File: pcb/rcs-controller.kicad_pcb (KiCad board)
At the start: 2 copper layers, 45.6 x 73 mm, 100 parts, among them J1 00222-32051, J10 0022-232021, J2 0022-232021, J3 0022-232041, J4 Screw_Terminal_4_P3.50mm, J5 USB_C_Receptacle_USB2.0_14P, J6 Conn_01x03, J8 00222-32051, Q1 SI7465DP-T1-E3, Q2 SI7465DP-T1-E3, Q3 SI7465DP-T1-E3, Q4 PMV45EN2, Q5 PMV45EN2, SW1 SW_Push, U1 LSM6DSOX, U2 MP26123DR-LF-Z, U3 TPS63070, U4 ESP32-S3-WROOM-1

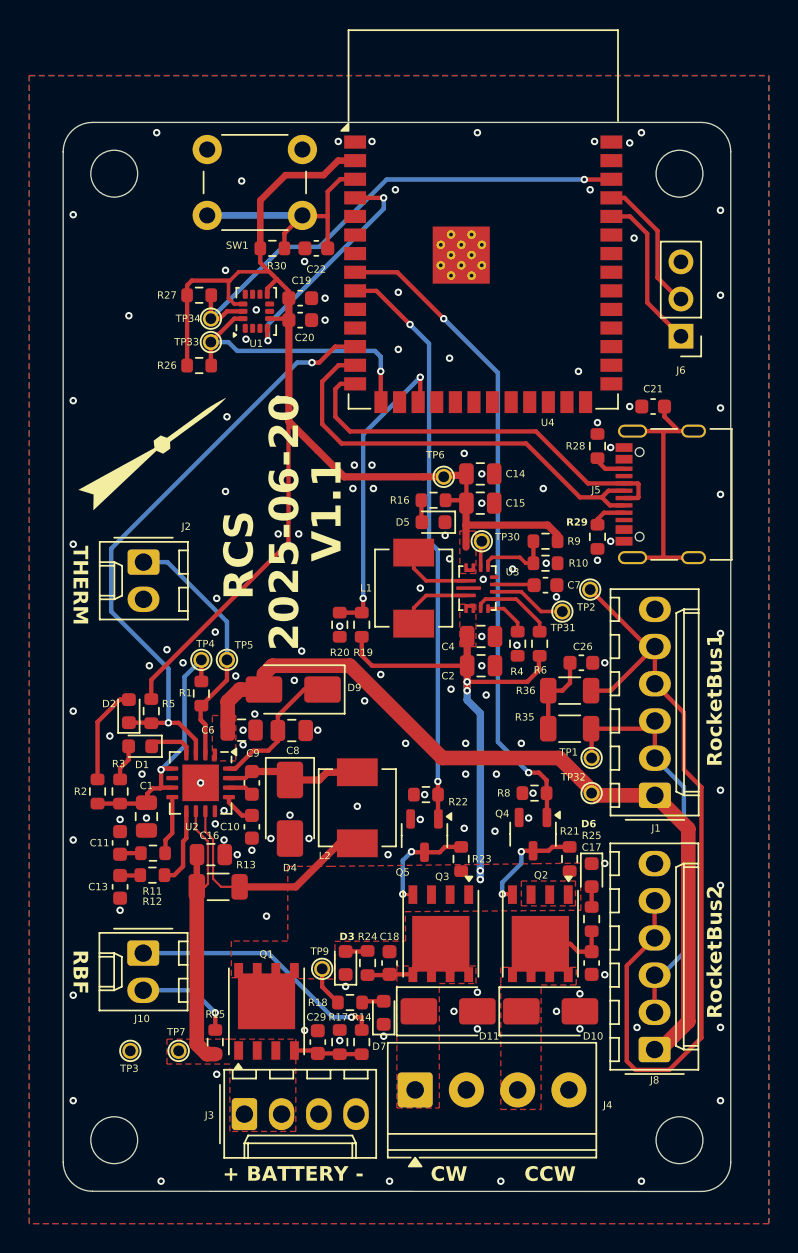
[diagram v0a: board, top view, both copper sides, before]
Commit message: added debug led and boot button
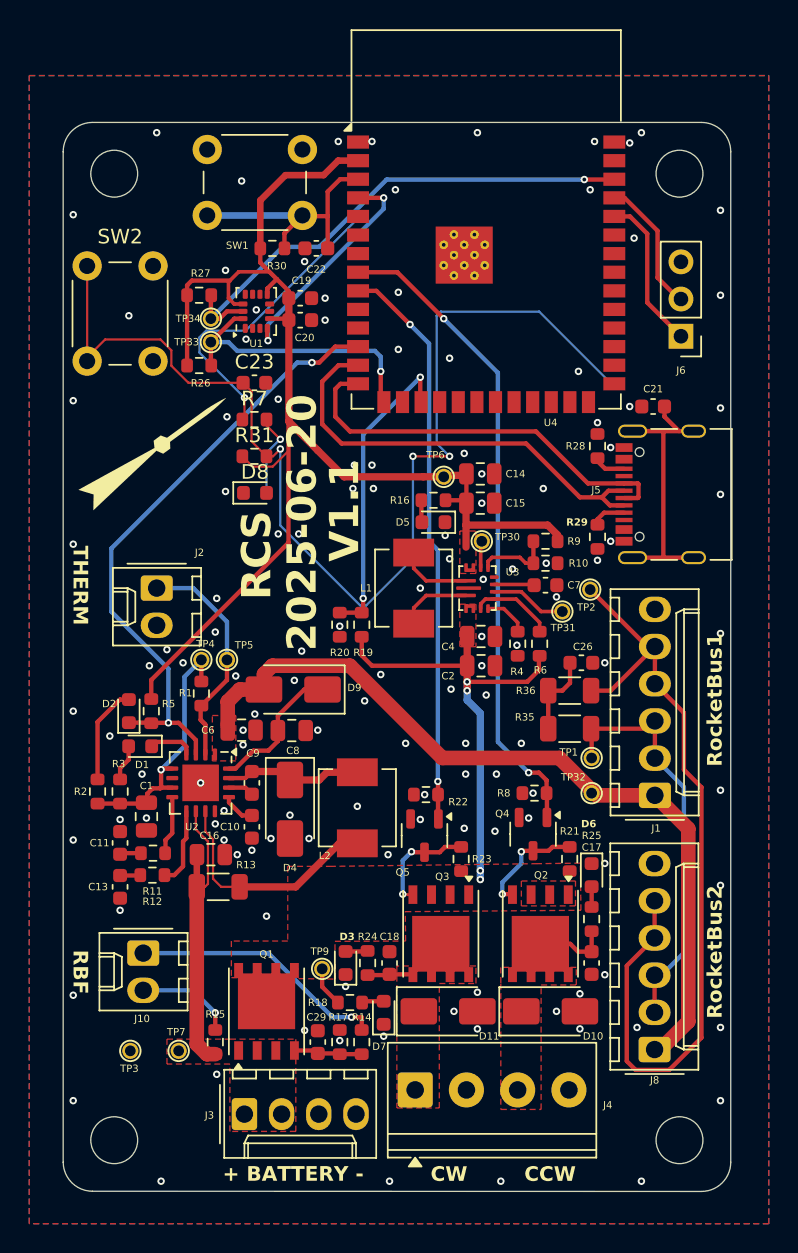
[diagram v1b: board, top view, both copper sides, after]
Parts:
- added C23: 100n, Capacitor_SMD:C_0603_1608Metric, F.Cu at (113.2, 96.0)
- added D8: Red, LED_SMD:LED_0603_1608Metric, F.Cu at (113.2, 103.5)
- added R31: 10k, Resistor_SMD:R_0603_1608Metric, F.Cu at (113.2, 101.0)
- added R7: 4.7, Resistor_SMD:R_0603_1608Metric, F.Cu at (113.2, 98.5)
- added SW2: SW_Push, Button_Switch_THT:SW_PUSH_6mm, F.Cu at (101.8, 94.5)
- C21: value 1p -> 100n
- C22: value 100p -> 100n
- R28, R29: value 5k -> 4.7k
- moved J2 1.99 mm to (106.5, 110.0)
- moved U4 0.20 mm to (129.0, 84.8)
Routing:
- net unconnected-(C23-Pad1): track 0.00 -> 77.7 mm, vias 0 -> 3
- net unconnected-(R7-Pad1): track 0.00 -> 21.5 mm, vias 0 -> 1
- net +3.3V: track 93.2 -> 99.2 mm
- net Net-(D8-A): track 0.00 -> 5.80 mm, vias 0 -> 1
- net Net-(J2-Pin_1): track 17.6 -> 16.0 mm

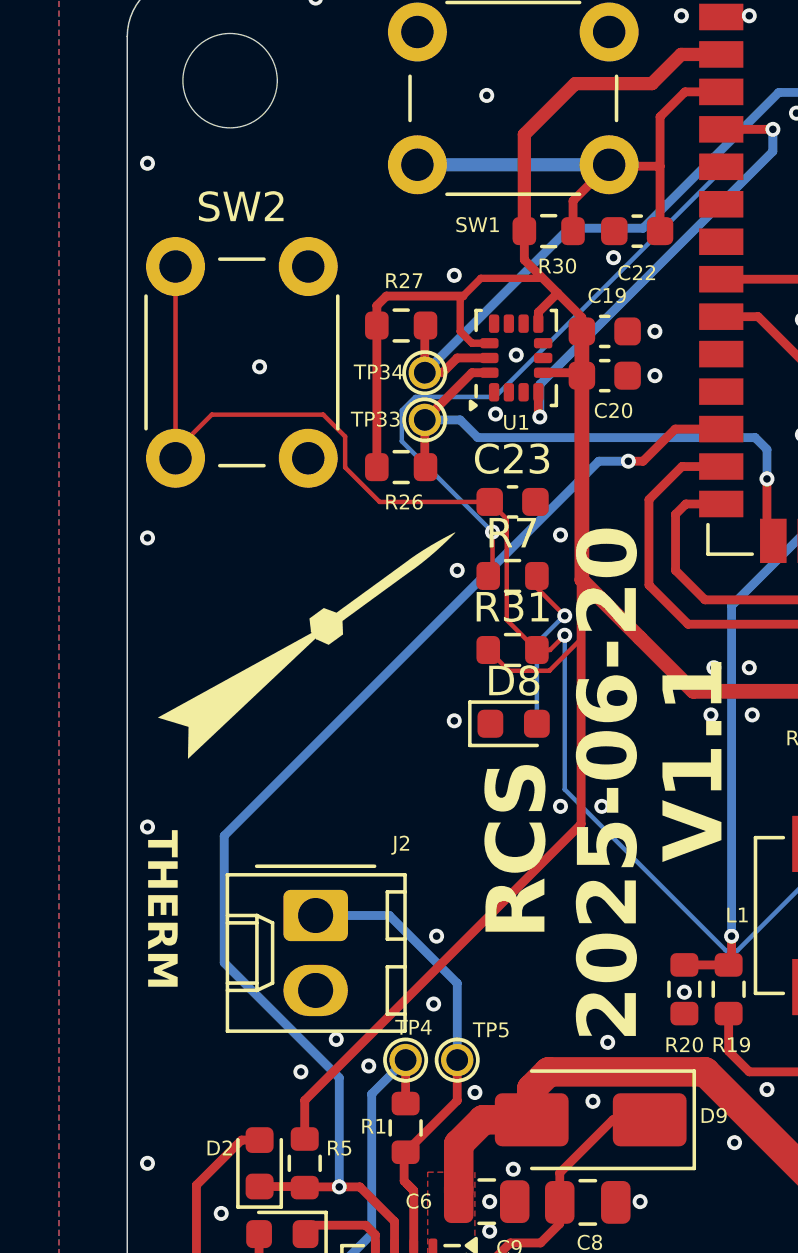
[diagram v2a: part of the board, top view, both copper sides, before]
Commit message: Potential switching circuit between battery and USB
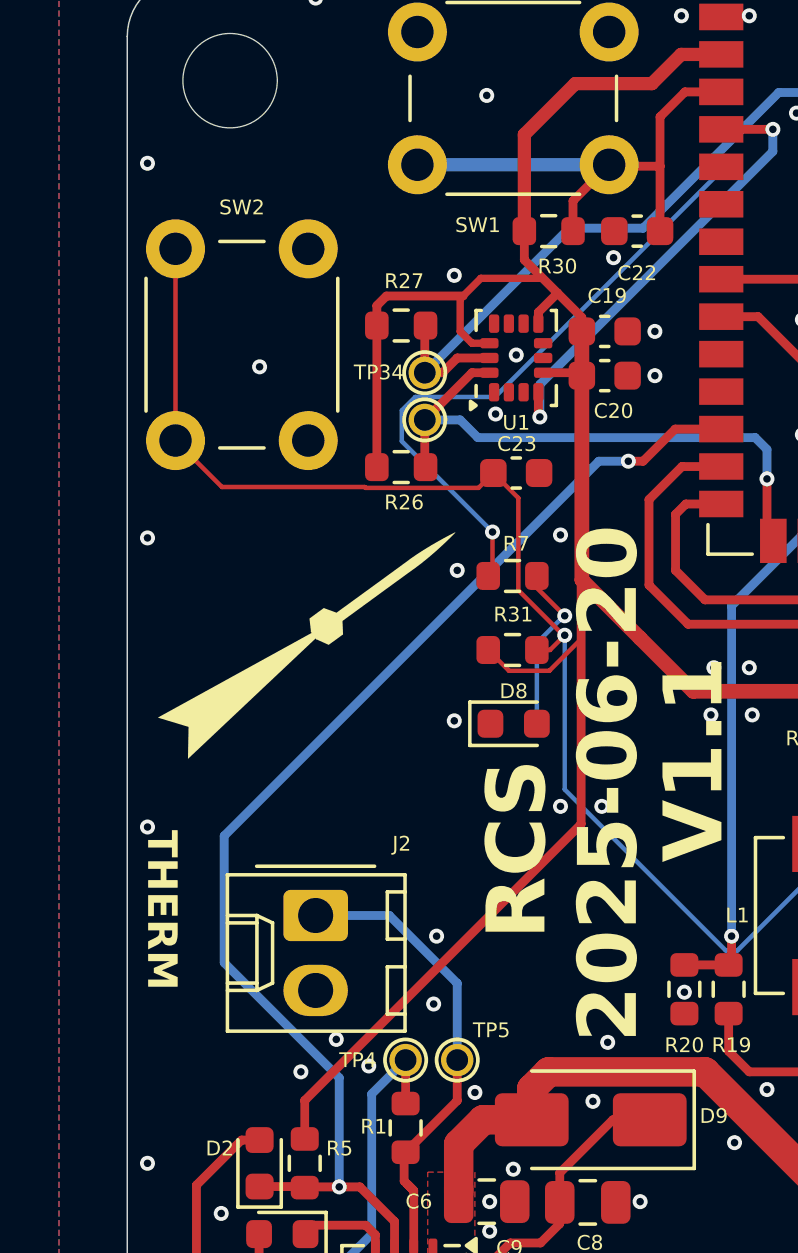
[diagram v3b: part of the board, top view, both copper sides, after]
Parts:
- moved C23 0.99 mm to (113.3, 95.0)
- moved SW2 0.60 mm to (101.8, 93.9)
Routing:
- net unconnected-(C23-Pad1): track 77.7 -> 77.2 mm
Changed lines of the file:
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@@
 		(tags "resistor")
 		(property "Reference" "R31"
-			(at 0 -1.43 0)
+			(at 0.025 -1.2 0)
 			(layer "F.SilkS")
 			(effects
 				(font
-					(size 1 1)
-					(thickness 0.15)
+					(size 0.5 0.5)
+					(thickness 0.125)
 				)
 			)
@@
 		)
 		(fp_text user "${REFERENCE}"
-			(at 0 0 0)
+			(at 0.6 -2.5 0)
 			(layer "F.Fab")
 			(effects
@@
 		(tags "LED")
 		(property "Reference" "D8"
-			(at 0 -1.43 0)
+			(at 0 -1.1 0)
 			(layer "F.SilkS")
 			(effects
 				(font
-					(size 1 1)
-					(thickness 0.15)
+					(size 0.5 0.5)
+					(thickness 0.125)
 				)
 			)
@@
 		(descr "Pin header test point")
 		(property "Reference" "TP4"
-			(at -0.35 -0.8 0)
+			(at -2.25 0.3 0)
 			(layer "F.SilkS")
 			(effects
@@
 	(footprint "Capacitor_SMD:C_0603_1608Metric"
 		(layer "F.Cu")
-		(at 113.175 95.98)
+		(at 113.3 95)
 		(descr "Capacitor SMD 0603 (1608 Metric), square (rectangular) end terminal, IPC-7351 nominal, (Body size source: IPC-SM-782 page 76, https://www.pcb-3d.com/wordpress/wp-content/uploads/ipc-sm-782a_amendment_1_and_2.pdf)")
 		(tags "capacitor")
 		(property "Reference" "C23"
-			(at 0 -1.43 0)
+			(at 0.025 -0.98 0)
 			(layer "F.SilkS")
 			(effects
 				(font
-					(size 1 1)
-					(thickness 0.15)
+					(size 0.5 0.5)
+					(thickness 0.125)
 				)
 			)
@@
 	(footprint "Button_Switch_THT:SW_PUSH_6mm"
 		(layer "F.Cu")
-		(at 101.75 94.5 90)
+		(at 101.75 93.9 90)
 		(descr "Generic 6mm SW tactile push button")
 		(tags "tact sw push 6mm")
 		(property "Reference" "SW2"
-			(at 8.5 2.25 180)
+			(at 7.9 2.25 180)
 			(layer "F.SilkS")
 			(effects
 				(font
-					(size 1 1)
-					(thickness 0.15)
+					(size 0.5 0.5)
+					(thickness 0.125)
 				)
 			)
@@
 		(tags "resistor")
 		(property "Reference" "R7"
-			(at 0 -1.43 0)
+			(at 0.125 -1.09 0)
 			(layer "F.SilkS")
 			(effects
 				(font
-					(size 1 1)
-					(thickness 0.15)
+					(size 0.5 0.5)
+					(thickness 0.125)
 				)
 			)
@@
 			(at -0.3 0.8 180)
 			(layer "F.SilkS")
+			(hide yes)
 			(effects
 				(font
@@
 	)
 	(segment
-		(start 107.5 94.811674)
-		(end 108.668326 95.98)
+		(start 108.191926 95.5036)
+		(end 112.0214 95.5036)
 		(width 0.1524)
 		(layer "F.Cu")
@@
 	)
 	(segment
-		(start 108.668326 95.98)
-		(end 112.4 95.98)
+		(start 113.3714 95.8464)
+		(end 113.3714 98.9714)
 		(width 0.1524)
 		(layer "F.Cu")
@@
 	)
 	(segment
-		(start 102.9786 93.0214)
-		(end 106.758903 93.0214)
+		(start 112.0214 95.5036)
+		(end 112.525 95)
 		(width 0.1524)
 		(layer "F.Cu")
@@
 	)
 	(segment
-		(start 106.758903 93.0214)
-		(end 107.5 93.762497)
+		(start 114.9 100.5)
+		(end 114.9436 100.5)
 		(width 0.1524)
 		(layer "F.Cu")
@@
 	)
 	(segment
-		(start 107.5 93.762497)
-		(end 107.5 94.811674)
+		(start 112.525 95)
+		(end 113.3714 95.8464)
 		(width 0.1524)
 		(layer "F.Cu")
@@
 	)
 	(segment
-		(start 112.4 95.98)
-		(end 112.9786 96.5586)
-		(width 0.1524)
-		(layer "F.Cu")
-		(net "unconnected-(C23-Pad1)")
-	)
-	(segment
 		(start 114 101)
 		(end 114.4436 101)
@@
 	)
 	(segment
-		(start 112.9786 96.5586)
-		(end 112.9786 99.9786)
+		(start 108.162151 95.473825)
+		(end 108.191926 95.5036)
 		(width 0.1524)
 		(layer "F.Cu")
@@
 	)
 	(segment
-		(start 112.9786 99.9786)
-		(end 114 101)
+		(start 113.3714 98.9714)
+		(end 114.9 100.5)
 		(width 0.1524)
 		(layer "F.Cu")
@@
 	)
 	(segment
-		(start 101.75 94.25)
-		(end 102.9786 93.0214)
+		(start 103.323825 95.473825)
+		(end 108.162151 95.473825)
+		(width 0.1524)
+		(layer "F.Cu")
+		(net "unconnected-(C23-Pad1)")
+	)
+	(segment
+		(start 101.75 93.9)
+		(end 103.323825 95.473825)
 		(width 0.1524)
 		(layer "F.Cu")

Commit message: power OR cleanup with Thomas for USB power
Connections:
- C23 pad 1: unconnected-(C23-Pad1) -> Net-(C23-Pad1)
- J5 pad A4: unconnected-(J5-VBUS-PadA4)_1 -> +5V
- J5 pad A9: unconnected-(J5-VBUS-PadA4)_2 -> +5V
- J5 pad B4: unconnected-(J5-VBUS-PadA4) -> +5V
- J5 pad B9: unconnected-(J5-VBUS-PadA4)_3 -> +5V
- R28 pad 1: Net-(J5-CC2) -> Net-(J5-CC1)
- R29 pad 1: Net-(J5-CC1) -> Net-(J5-CC2)
- R31 pad 2: unconnected-(C23-Pad1) -> Net-(C23-Pad1)
- R7 pad 1: unconnected-(R7-Pad1) -> Net-(U4-IO5)
- SW2 pad 1: unconnected-(C23-Pad1) -> Net-(U4-IO0)
- U4 pad 27: unconnected-(C23-Pad1) -> Net-(U4-IO0)
- U4 pad 5: unconnected-(R7-Pad1) -> Net-(U4-IO5)
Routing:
- net unconnected-(C23-Pad1): track 77.2 -> 0.00 mm, vias 3 -> 0
- net (no net): track 0.00 -> 77.2 mm, vias 0 -> 3
- net unconnected-(R7-Pad1): track 21.5 -> 0.00 mm, vias 1 -> 0
- net Net-(U4-IO5): track 0.00 -> 21.5 mm, vias 0 -> 1

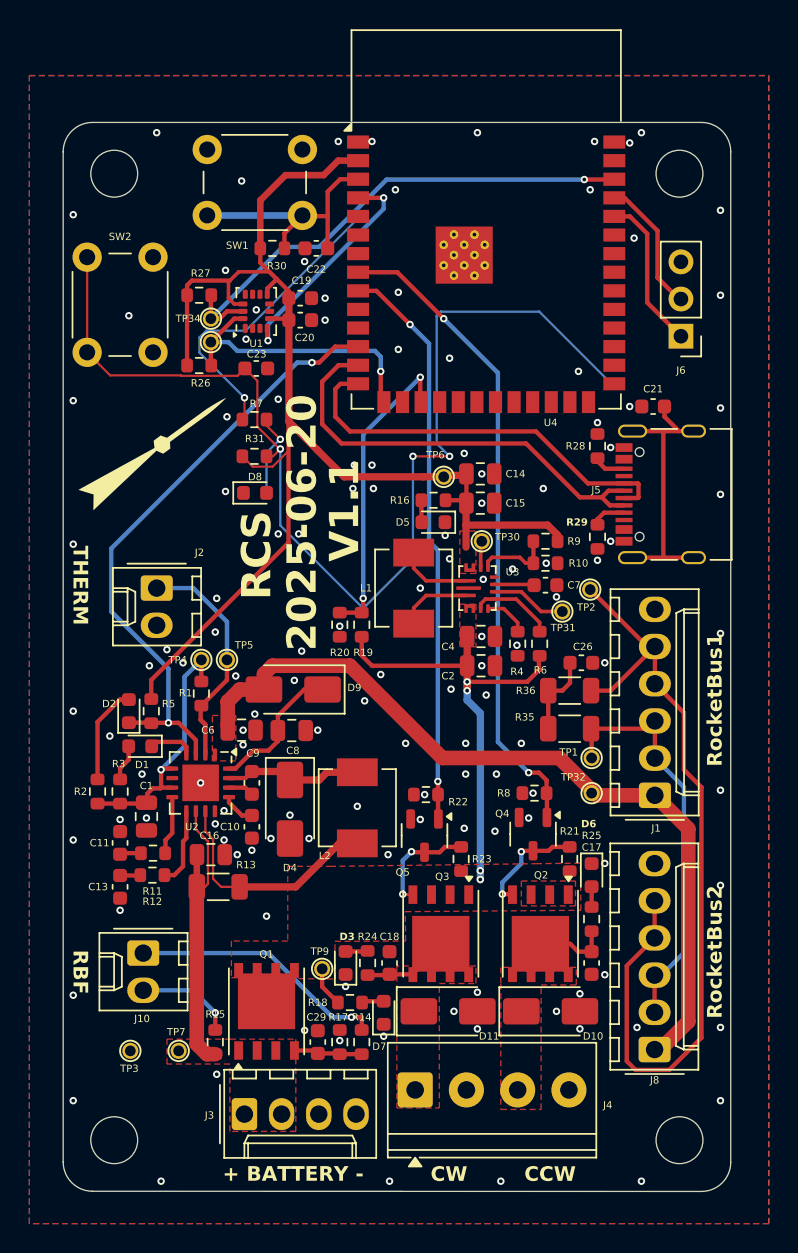
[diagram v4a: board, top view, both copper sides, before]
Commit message: Added Andrew's new power switching diode and removed some unconnected traces
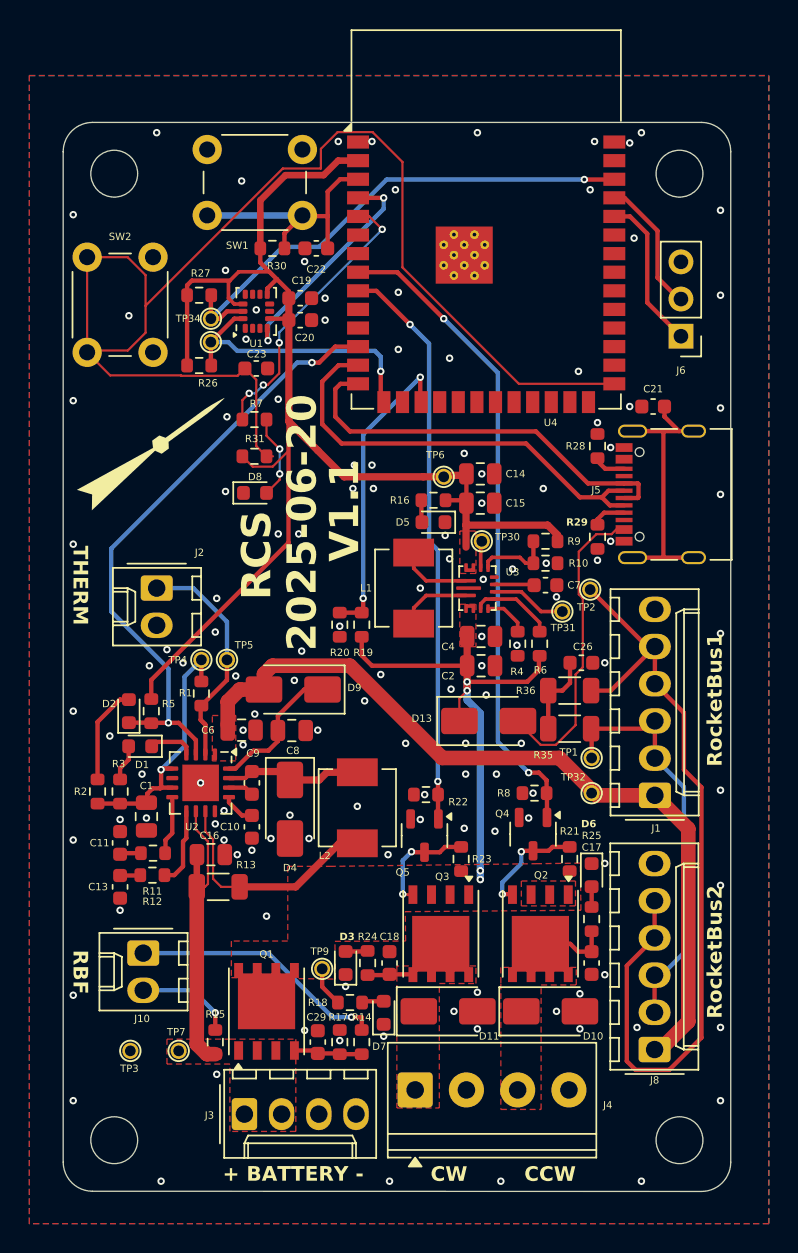
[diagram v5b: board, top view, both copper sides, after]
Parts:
- added D13: RBR5L30BDDTE25, Diode_SMD:D_SMA, F.Cu at (129.2, 119.1)
- moved LOGO1 0.10 mm to (106.4, 100.5)
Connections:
- R28 pad 1: Net-(J5-CC1) -> Net-(J5-CC2)
- R29 pad 1: Net-(J5-CC2) -> Net-(J5-CC1)
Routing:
- net Net-(U4-IO0): track 0.00 -> 61.7 mm
- net (no net): track 77.2 -> 18.1 mm, vias 3 -> 0
- net +5V: track 0.00 -> 21.1 mm
- net Net-(C23-Pad1): track 0.00 -> 6.75 mm
- net VBUS: track 35.5 -> 37.8 mm
- net Net-(U4-IO5): track 21.5 -> 19.6 mm, vias 1 -> 4
- net Net-(D8-A): track 5.80 -> 5.76 mm, vias 1 -> 2

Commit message: Added ports to transducer and power switch
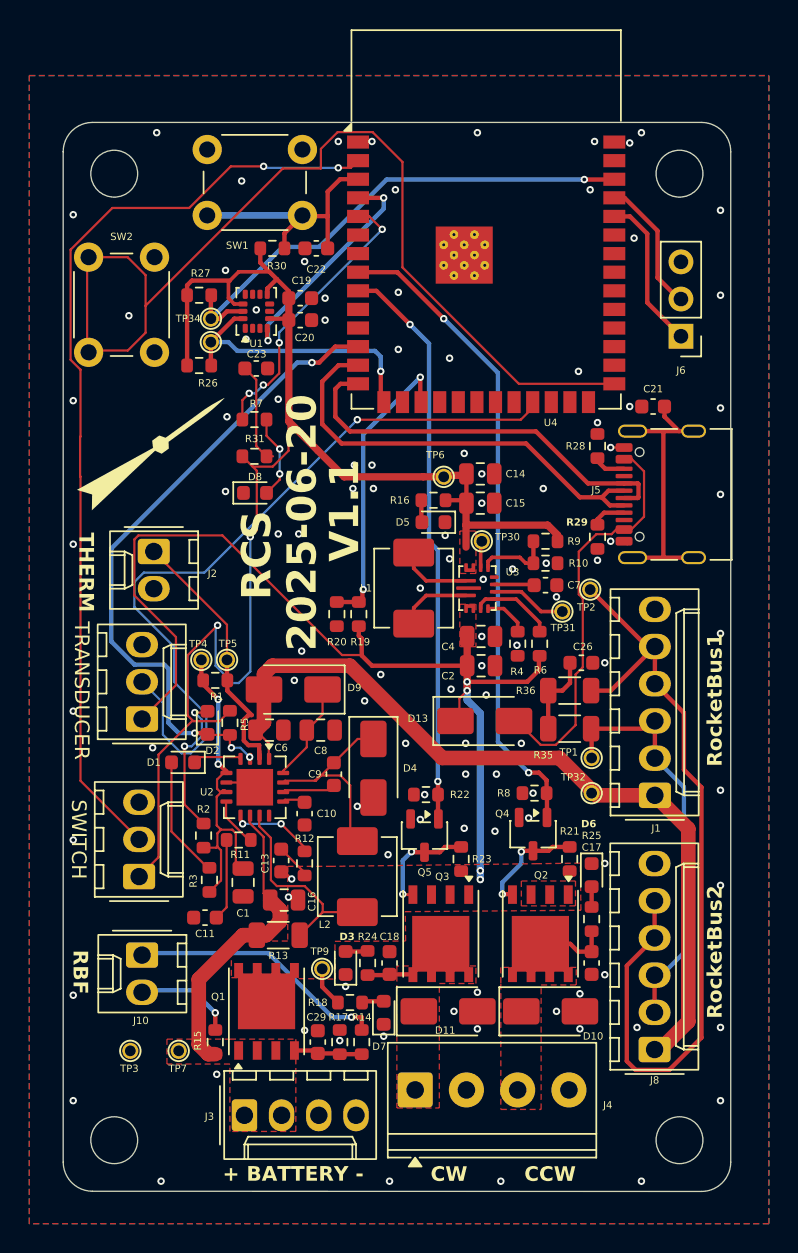
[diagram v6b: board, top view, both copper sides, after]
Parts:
- added SWITCH: Conn_01x03, Connector_Molex:Molex_KK-254_AE-6410-03A_1x03_P2.54mm_Vertical, F.Cu at (105.3, 129.7)
- added TRANSDUCER: Conn_01x03, Connector_Molex:Molex_KK-254_AE-6410-03A_1x03_P2.54mm_Vertical, F.Cu at (105.5, 118.9)
- moved C13 11.1 mm to (115.0, 128.6)
- moved R12 10.4 mm to (116.6, 128.8), turned to -90 degrees
- moved R3 8.58 mm to (110.1, 129.9)
- moved C1 7.99 mm to (112.4, 130.1)
- moved R2 7.84 mm to (109.7, 126.9)
- moved C11 7.72 mm to (109.8, 132.5), turned to 180 degrees
- moved D4 6.35 mm to (121.3, 122.3)
- moved R11 5.92 mm to (112.1, 127.2)
- moved C16 5.88 mm to (115.2, 131.3)
- moved C9 5.63 mm to (118.6, 122.7)
- moved D2 5.43 mm to (110.0, 119.2)
- moved R5 5.43 mm to (111.5, 119.2)
- moved R13 5.26 mm to (114.8, 133.7)
- moved L2 4.70 mm to (120.2, 129.7)
- moved U2 3.71 mm to (113.2, 123.6)
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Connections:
- U4 pad 2: +3.3V -> Net-(J9-Pin_2)
- U4 pad 23: unconnected-(U4-IO21-Pad23) -> Net-(J11-Pin_2)
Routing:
- net Net-(J9-Pin_2): track 0.00 -> 64.5 mm, vias 0 -> 2
- net Net-(J11-Pin_2): track 0.00 -> 53.3 mm, vias 0 -> 1
- net VBUS: track 37.8 -> 72.2 mm
- net (no net): track 18.1 -> 0.00 mm
- net +3.3V: track 99.2 -> 110.0 mm, vias 0 -> 2
- net +5V: track 21.1 -> 27.8 mm
- net Net-(U4-IO0): track 61.7 -> 68.2 mm
- net Net-(D1-A): track 2.51 -> 8.34 mm
- net /Power/VREF33: track 17.9 -> 23.4 mm, vias 1 -> 2
- net GND: track 0.16 -> 5.05 mm, vias 130 -> 107
- net Net-(D4-K): track 9.47 -> 14.2 mm
- net Net-(C11-Pad1): track 1.35 -> 5.59 mm
- net Net-(D2-A): track 6.70 -> 9.99 mm, vias 0 -> 2
- net Net-(D9-K): track 9.70 -> 6.81 mm
- net Net-(J2-Pin_1): track 16.0 -> 18.7 mm
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- removed copper zone on F.Cu, net /Power/VUMB
